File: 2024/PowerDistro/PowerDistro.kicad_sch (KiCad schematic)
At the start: 0 parts

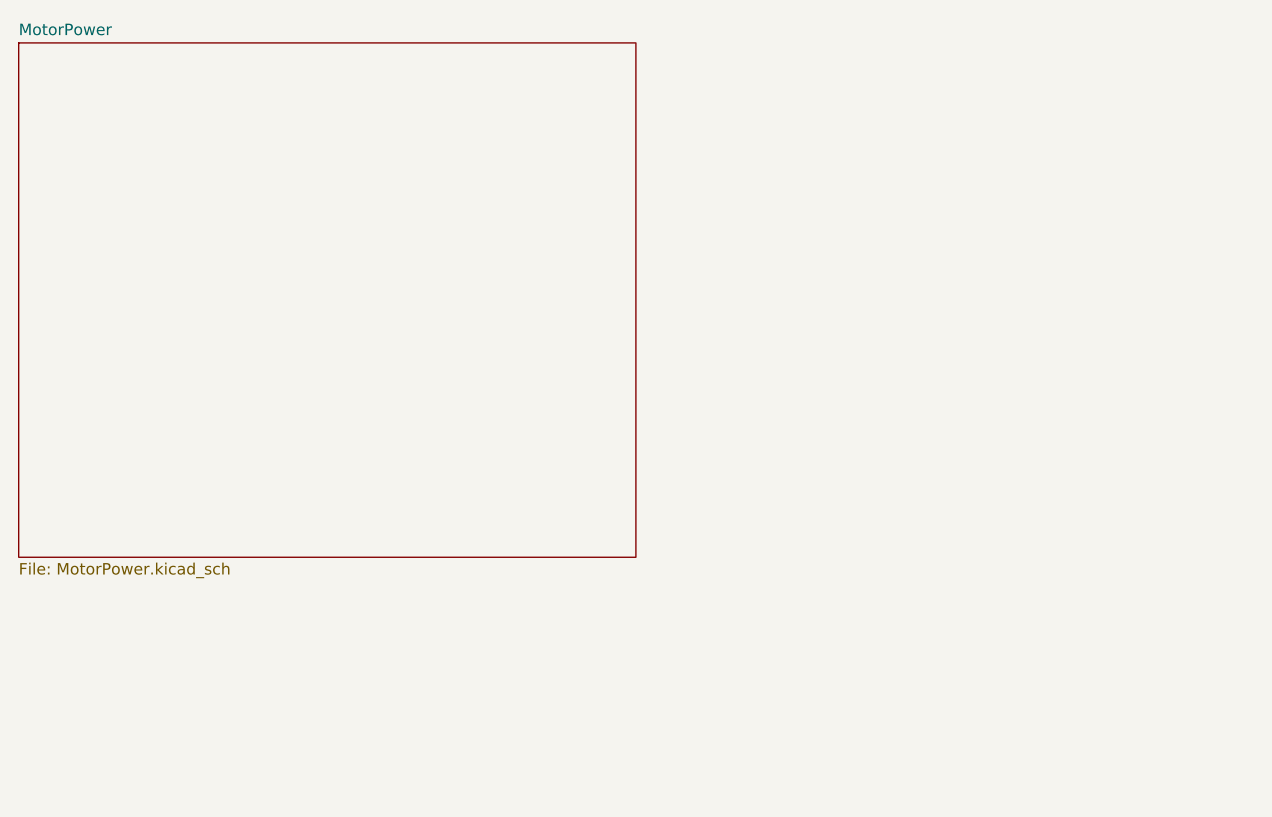
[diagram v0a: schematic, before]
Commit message: Added all other motor power distribution junctions
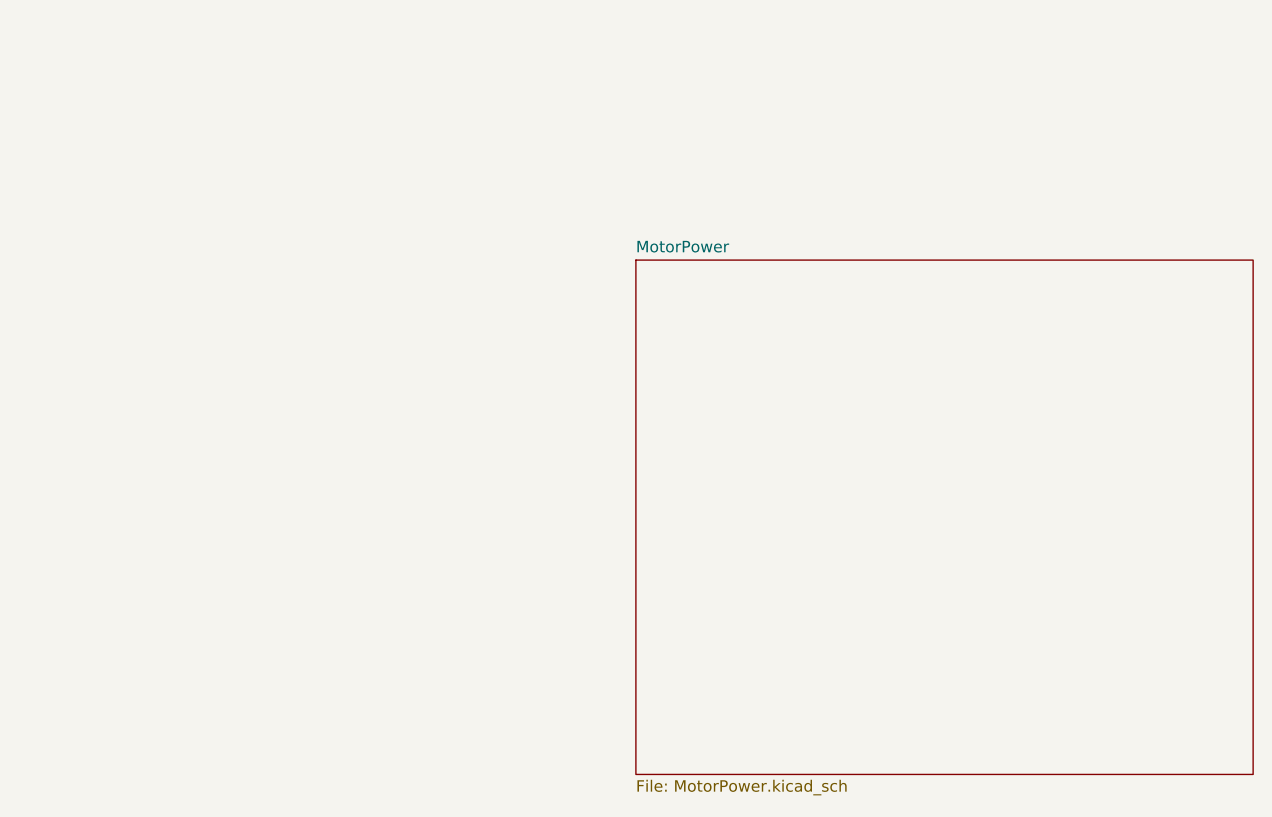
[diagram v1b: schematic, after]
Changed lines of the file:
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@@
 	(paper "A4")
 	(sheet
-		(at 144.78 81.28)
+		(at 213.36 105.41)
 		(size 68.58 57.15)
 		(fields_autoplaced yes)
@@
 		)
 		(property "Sheetname" "MotorPower"
-			(at 144.78 80.5684 0)
+			(at 213.36 104.6984 0)
 			(effects
 				(font
@@
 		)
 		(property "Sheetfile" "MotorPower.kicad_sch"
-			(at 144.78 139.0146 0)
+			(at 213.36 163.1446 0)
 			(effects
 				(font

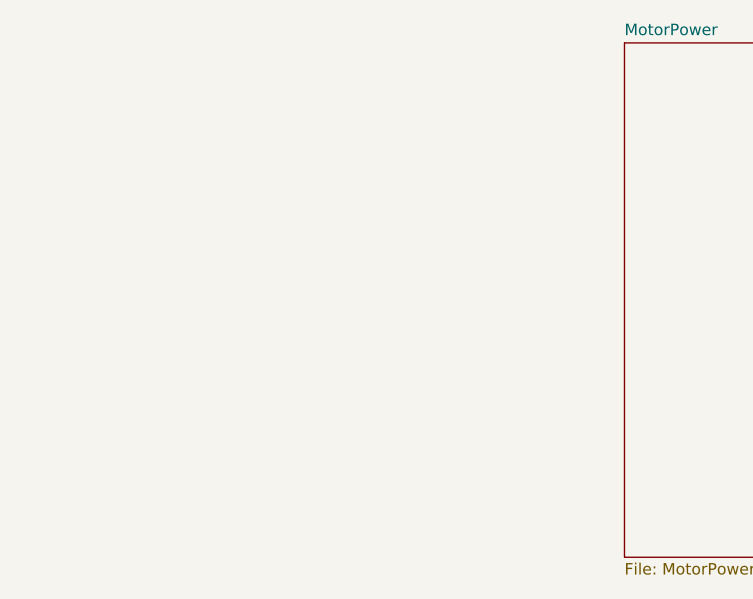
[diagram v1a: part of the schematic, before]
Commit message: Added jetson pinout on to main schematic
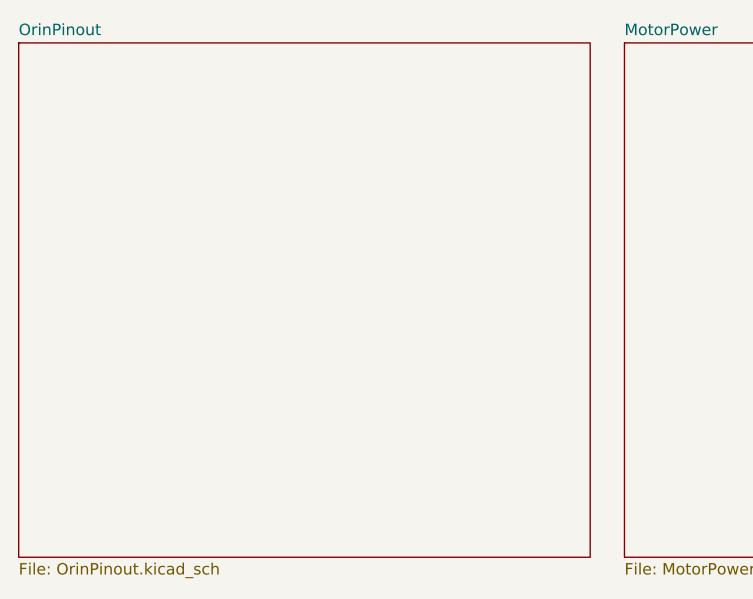
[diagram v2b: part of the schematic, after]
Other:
- added sheet OrinPinout (OrinPinout.kicad_sch)
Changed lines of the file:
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@@
 	(paper "A4")
+	(sheet
+		(at 146.05 105.41)
+		(size 63.5 57.15)
+		(fields_autoplaced yes)
+		(stroke
+			(width 0.1524)
+			(type solid)
+		)
+		(fill
+			(color 0 0 0 0.0000)
+		)
+		(property "Sheetname" "OrinPinout"
+			(at 146.05 104.6984 0)
+			(effects
+				(font
+					(size 1.27 1.27)
+				)
+				(justify left bottom)
+			)
+		)
+		(property "Sheetfile" "OrinPinout.kicad_sch"
+			(at 146.05 163.1446 0)
+			(effects
+				(font
+					(size 1.27 1.27)
+				)
+				(justify left top)
+			)
+		)
+		(instances
+			(project "PowerDistro"
+				(path "/605eff46-b281-4cd5-84ac-aa97178bb7be"
+					(page "3")
+				)
+			)
+		)
+	)
 	(sheet
 		(at 213.36 105.41)

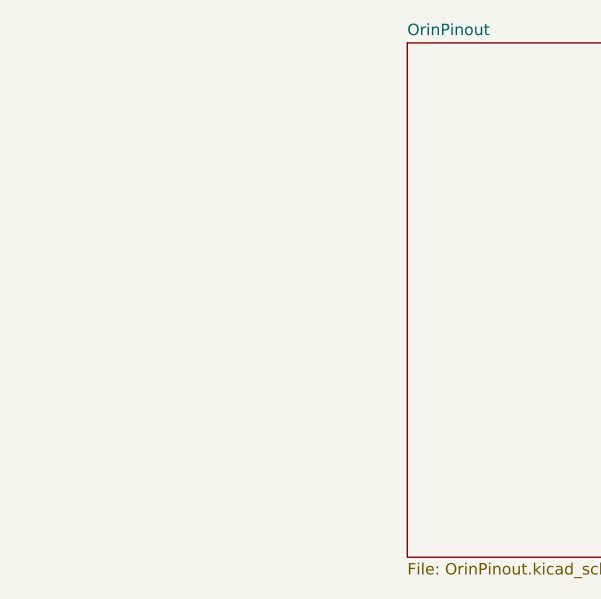
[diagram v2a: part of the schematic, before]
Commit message: Added PCA 9862 to Power distro schematic and started PCB
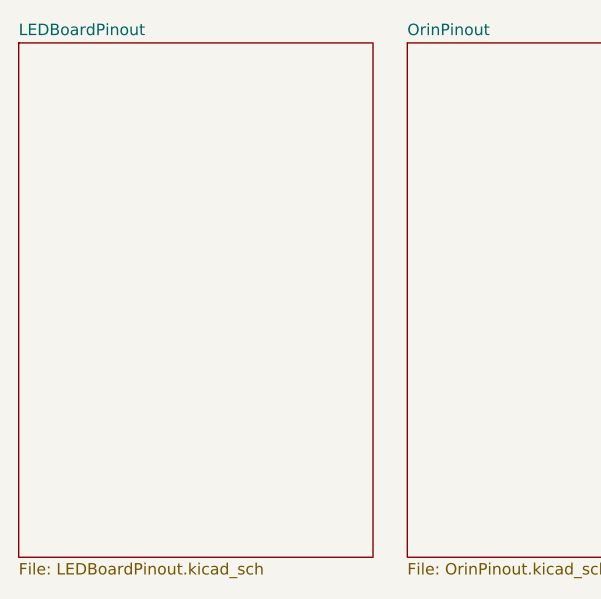
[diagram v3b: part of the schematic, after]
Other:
- added sheet LEDBoardPinout (LEDBoardPinout.kicad_sch)
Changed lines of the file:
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@@
+	)
+	(sheet
+		(at 102.87 105.41)
+		(size 39.37 57.15)
+		(fields_autoplaced yes)
+		(stroke
+			(width 0.1524)
+			(type solid)
+		)
+		(fill
+			(color 0 0 0 0.0000)
+		)
+		(property "Sheetname" "LEDBoardPinout"
+			(at 102.87 104.6984 0)
+			(effects
+				(font
+					(size 1.27 1.27)
+				)
+				(justify left bottom)
+			)
+		)
+		(property "Sheetfile" "LEDBoardPinout.kicad_sch"
+			(at 102.87 163.1446 0)
+			(effects
+				(font
+					(size 1.27 1.27)
+				)
+				(justify left top)
+			)
+		)
+		(instances
+			(project "PowerDistro"
+				(path "/605eff46-b281-4cd5-84ac-aa97178bb7be"
+					(page "4")
+				)
+			)
+		)
 	)
 	(sheet

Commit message: saved i guess idk
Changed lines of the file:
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@@
 	)
 	(sheet
-		(at 102.87 105.41)
-		(size 39.37 57.15)
+		(at 81.28 105.41)
+		(size 60.96 57.15)
 		(fields_autoplaced yes)
 		(stroke
@@
 		)
 		(property "Sheetname" "LEDBoardPinout"
-			(at 102.87 104.6984 0)
+			(at 81.28 104.6984 0)
 			(effects
 				(font
@@
 		)
 		(property "Sheetfile" "LEDBoardPinout.kicad_sch"
-			(at 102.87 163.1446 0)
+			(at 81.28 163.1446 0)
 			(effects
 				(font

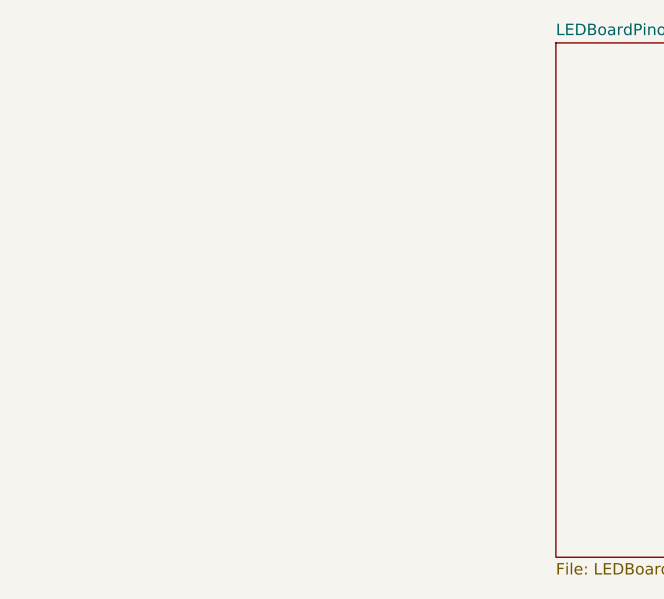
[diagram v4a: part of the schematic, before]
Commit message: Added connectors and esc footprints
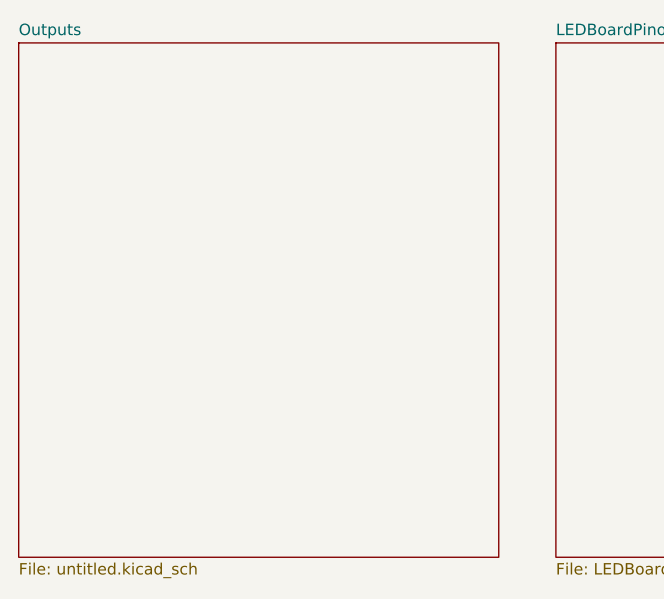
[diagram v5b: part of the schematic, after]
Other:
- added sheet Outputs (untitled.kicad_sch)
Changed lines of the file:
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@@
+	)
+	(sheet
+		(at 21.59 105.41)
+		(size 53.34 57.15)
+		(fields_autoplaced yes)
+		(stroke
+			(width 0.1524)
+			(type solid)
+		)
+		(fill
+			(color 0 0 0 0.0000)
+		)
+		(property "Sheetname" "Outputs"
+			(at 21.59 104.6984 0)
+			(effects
+				(font
+					(size 1.27 1.27)
+				)
+				(justify left bottom)
+			)
+		)
+		(property "Sheetfile" "untitled.kicad_sch"
+			(at 21.59 163.1446 0)
+			(effects
+				(font
+					(size 1.27 1.27)
+				)
+				(justify left top)
+			)
+		)
+		(instances
+			(project "PowerDistro"
+				(path "/605eff46-b281-4cd5-84ac-aa97178bb7be"
+					(page "5")
+				)
+			)
+		)
 	)
 	(sheet

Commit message: Changed Everything
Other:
- sheet LEDBoardPinout renamed PWM Driver
- sheet OrinPinout renamed Jetson Orin
- sheet Outputs renamed Motor Drivers
- removed sheet MotorPower
- added sheet Solonoid Switches (SolonoidSwitches.kicad_sch)
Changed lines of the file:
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@@
 	(paper "A4")
 	(sheet
-		(at 146.05 105.41)
+		(at 184.15 73.66)
 		(size 63.5 57.15)
 		(fields_autoplaced yes)
@@
 			(color 0 0 0 0.0000)
 		)
-		(property "Sheetname" "OrinPinout"
-			(at 146.05 104.6984 0)
+		(property "Sheetname" "Jetson Orin"
+			(at 184.15 72.9484 0)
 			(effects
 				(font
@@
 		)
 		(property "Sheetfile" "OrinPinout.kicad_sch"
-			(at 146.05 163.1446 0)
+			(at 184.15 131.3946 0)
 			(effects
 				(font
@@
 	)
 	(sheet
-		(at 21.59 105.41)
-		(size 53.34 57.15)
+		(at 45.72 73.66)
+		(size 67.31 57.15)
 		(fields_autoplaced yes)
 		(stroke
@@
 			(color 0 0 0 0.0000)
 		)
-		(property "Sheetname" "Outputs"
-			(at 21.59 104.6984 0)
+		(property "Sheetname" "Motor Drivers"
+			(at 45.72 72.9484 0)
 			(effects
 				(font
@@
 		)
 		(property "Sheetfile" "untitled.kicad_sch"
-			(at 21.59 163.1446 0)
+			(at 45.72 131.3946 0)
 			(effects
 				(font
@@
 	)
 	(sheet
-		(at 81.28 105.41)
+		(at 119.38 73.66)
 		(size 60.96 57.15)
 		(fields_autoplaced yes)
@@
 			(color 0 0 0 0.0000)
 		)
-		(property "Sheetname" "LEDBoardPinout"
-			(at 81.28 104.6984 0)
+		(property "Sheetname" "PWM Driver"
+			(at 119.38 72.9484 0)
 			(effects
 				(font
@@
 		)
 		(property "Sheetfile" "LEDBoardPinout.kicad_sch"
-			(at 81.28 163.1446 0)
+			(at 119.38 131.3946 0)
 			(effects
 				(font
@@
 	)
 	(sheet
-		(at 213.36 105.41)
-		(size 68.58 57.15)
+		(at 203.2 33.02)
+		(size 57.15 33.02)
 		(fields_autoplaced yes)
 		(stroke
@@
 			(color 0 0 0 0.0000)
 		)
-		(property "Sheetname" "MotorPower"
-			(at 213.36 104.6984 0)
+		(property "Sheetname" "Solonoid Switches"
+			(at 203.2 32.3084 0)
 			(effects
 				(font
@@
 			)
 		)
-		(property "Sheetfile" "MotorPower.kicad_sch"
-			(at 213.36 163.1446 0)
+		(property "Sheetfile" "SolonoidSwitches.kicad_sch"
+			(at 203.2 66.6246 0)
 			(effects
 				(font
@@
 			(project "PowerDistro"
 				(path "/605eff46-b281-4cd5-84ac-aa97178bb7be"
-					(page "2")
+					(page "5")
 				)
 			)
